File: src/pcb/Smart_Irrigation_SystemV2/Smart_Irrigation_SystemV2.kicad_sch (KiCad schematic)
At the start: 110 parts, among them J1 USB_C_Receptacle_USB2.0_16P, J2 FPC_Connector, J3 AudioJack3, J4 AudioJack3, J5 AudioJack3, J7 AudioJack3, J8 AudioJack3, J9 Battary Connection, Q1 MUN5211DW1, Q2 FDN340P, Q3 AO3400A, SW1 IO0 Switch, SW2 EN Switch, SW3 SW_Push, SW4 SW_Push, SW5 SW_Push, SW6 SW_Push, U1 CP2102N-Axx-xQFN28, U2 ESP32-WROOM-32, U3 ADS1115IDGS, U4 DS3231MZ, U5 TLV62568ADRL, U6 SN74LVC245APW, U7 TP4056-42-ESOP8, U8 TPS63001, U9 AT24CS32-SSHM

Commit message: set footprints, added TestPoints, searched JLCPCB Parts
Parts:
- added J10, J11, J6: I2C, Connector_PinSocket_2.54mm:PinSocket_1x04_P2.54mm_Vertical, symbol Connector:Conn_01x04_Socket
- added TP15: GND, TestPoint:TestPoint_Pad_2.5x2.5mm, symbol Connector:TestPoint
- added TP16: 3.3V, TestPoint:TestPoint_Pad_4.0x4.0mm, symbol Connector:TestPoint
- C1, C10, C11, C2, C4, C8, C9: footprint (none) -> Capacitor_SMD:C_0805_2012Metric; JLCPCB Part Number (none) -> C28233
- C12, C13, C14: footprint (none) -> Capacitor_SMD:C_0805_2012Metric; JLCPCB Part Number (none) -> C15850
- C3, C5, C6: footprint (none) -> Capacitor_SMD:C_0805_2012Metric; JLCPCB Part Number (none) -> C1779
- C7: footprint (none) -> Capacitor_SMD:C_0805_2012Metric; JLCPCB Part Number (none) -> C45783
- D1, D11, D12, D15, D16, D17, D2, D3: JLCPCB Part Number (none) -> C5274290
- D10: JLCPCB Part Number (none) -> C5355496
- D4: footprint Package_TO_SOT_SMD:SOT-23-5 -> Diode_SMD:D_SOD-323F; JLCPCB Part Number (none) -> C27636120
- D5, D6, D7: footprint LED_SMD:LED_Cree-XHP50_3V_HighDensity -> Diode_SMD:D_0603_1608Metric; JLCPCB Part Number (none) -> C2286
- D8: footprint LED_SMD:LED_Cree-XHP50_3V_HighDensity -> Diode_SMD:D_0603_1608Metric; JLCPCB Part Number (none) -> C2287
- D9: footprint LED_SMD:LED_Cree-XHP50_3V_HighDensity -> Diode_SMD:D_0603_1608Metric; JLCPCB Part Number (none) -> C12624
- H1, H2, H3, H4: footprint Module:Maple_Mini -> MountingHole:MountingHole_3.2mm_M3_DIN965_Pad
- J1: footprint Package_DFN_QFN:UQFN-16_1.8x2.6mm_P0.4mm -> Connector_USB:USB_C_Receptacle_HRO_TYPE-C-31-M-12; JLCPCB Part Number (none) -> C5337088
- J2: footprint Package_QFP:TQFP-144_20x20mm_P0.5mm -> 5051105091:CON_5051105091_MOL; JLCPCB Part Number (none) -> C779387
- J3, J4, J5, J7, J8: footprint Package_LCC:PLCC-84_29.3x29.3mm_P1.27mm -> (none); JLCPCB Part Number (none) -> C707248
- J9: footprint Package_QFP:TQFP-144_20x20mm_P0.5mm -> Connector_JST:JST_PH_B2B-PH-K_1x02_P2.00mm_Vertical
- L1: footprint Package_TO_SOT_SMD:SOT-563 -> Inductor_SMD:L_7.3x7.3_H3.5; JLCPCB Part Number (none) -> C726315
- L2: footprint Relay_THT:Relay_DPDT_Finder_30.22 -> Inductor_SMD:L_7.3x7.3_H3.5; JLCPCB Part Number (none) -> C128686
- MICRO_SD1: JLCPCB Part Number (none) -> C91145
- Q1: JLCPCB Part Number (none) -> C152507
- Q2: JLCPCB Part Number (none) -> C347510
- Q3: JLCPCB Part Number (none) -> C20917
- R1, R2: footprint Resistor_THT:R_Array_SIP4 -> Resistor_SMD:R_0805_2012Metric; JLCPCB Part Number (none) -> C26023
- R10, R11, R12, R13, R14, R15: footprint Resistor_THT:R_Array_SIP4 -> Resistor_SMD:R_0805_2012Metric; JLCPCB Part Number (none) -> C17415
- R16: footprint Resistor_THT:R_Array_SIP4 -> Resistor_SMD:R_0805_2012Metric; JLCPCB Part Number (none) -> C17477
- R17, R5: footprint Resistor_THT:R_Array_SIP4 -> Resistor_SMD:R_0805_2012Metric; JLCPCB Part Number (none) -> C17414
- R18, R19, R4: footprint (none) -> Resistor_SMD:R_0805_2012Metric; JLCPCB Part Number (none) -> C17673
- R20, R21, R22, R23: footprint Resistor_THT:R_Array_SIP4 -> Resistor_SMD:R_0805_2012Metric; JLCPCB Part Number (none) -> C17513
- R24: footprint (none) -> Resistor_SMD:R_0805_2012Metric; JLCPCB Part Number (none) -> C17414
- R25, R26, R27: footprint Package_SON:Texas_DRC0010J_ThermalVias -> Resistor_SMD:R_0805_2012Metric; JLCPCB Part Number (none) -> C17604
- R28: footprint Package_SON:Texas_DRC0010J_ThermalVias -> Resistor_SMD:R_0805_2012Metric; JLCPCB Part Number (none) -> C17408
- R29: footprint Package_SON:Texas_DRC0010J_ThermalVias -> Resistor_SMD:R_0805_2012Metric; JLCPCB Part Number (none) -> C25611
- R3: footprint Resistor_THT:R_Array_SIP4 -> Resistor_SMD:R_0805_2012Metric; JLCPCB Part Number (none) -> C17520
- R30, R31, R32: footprint Package_SON:Texas_DRC0010J_ThermalVias -> Resistor_SMD:R_0805_2012Metric; JLCPCB Part Number (none) -> C17414
- R33, R34: footprint (none) -> Resistor_SMD:R_0805_2012Metric; JLCPCB Part Number (none) -> C17477
- R6, R7: footprint (none) -> Resistor_SMD:R_0805_2012Metric; JLCPCB Part Number (none) -> C17513
- R8: footprint Resistor_THT:R_Array_SIP4 -> Resistor_SMD:R_0805_2012Metric; JLCPCB Part Number (none) -> C17702
- R9: footprint (none) -> Resistor_SMD:R_0805_2012Metric; JLCPCB Part Number (none) -> C25611
- SW1, SW2: footprint Button_Switch_THT:SW_NKK_GW12LJP -> (none); JLCPCB Part Number (none) -> C83206
- SW3, SW4, SW5, SW6: footprint Button_Switch_THT:SW_NKK_GW12LJP -> (none); JLCPCB Part Number (none) -> C49234238
- TP1: value TestPoint -> GPIO32; footprint Package_SO:TSSOP-16_4.4x5mm_P0.65mm -> TestPoint:TestPoint_Pad_D1.5mm
- TP10, TP11, TP12, TP13, TP14, TP4, TP5, TP6, TP7, TP8, TP9: footprint (none) -> TestPoint:TestPoint_Pad_D1.5mm
- TP2, TP3: footprint Package_SO:TSSOP-16_4.4x5mm_P0.65mm -> TestPoint:TestPoint_Pad_D1.5mm
- U1: JLCPCB Part Number (none) -> C964632
- U2: JLCPCB Part Number (none) -> C701343
- U3: JLCPCB Part Number (none) -> C37593
- U4: JLCPCB Part Number (none) -> C107410
- U5: JLCPCB Part Number (none) -> C87122
- U6: JLCPCB Part Number (none) -> C7848
- U7: JLCPCB Part Number (none) -> C16581
- U8: JLCPCB Part Number (none) -> C28060
- U9: JLCPCB Part Number (none) -> C615972
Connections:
- net +3.3V: now also J10.4 (Pin_4), J11.4 (Pin_4), J6.4 (Pin_4), TP16.1
- net GND: now also J10.3 (Pin_3), J11.3 (Pin_3), J6.3 (Pin_3), TP15.1
- net SCL: now also J10.1 (Pin_1), J11.1 (Pin_1), J6.1 (Pin_1)
- net SDA: now also J10.2 (Pin_2), J11.2 (Pin_2), J6.2 (Pin_2)

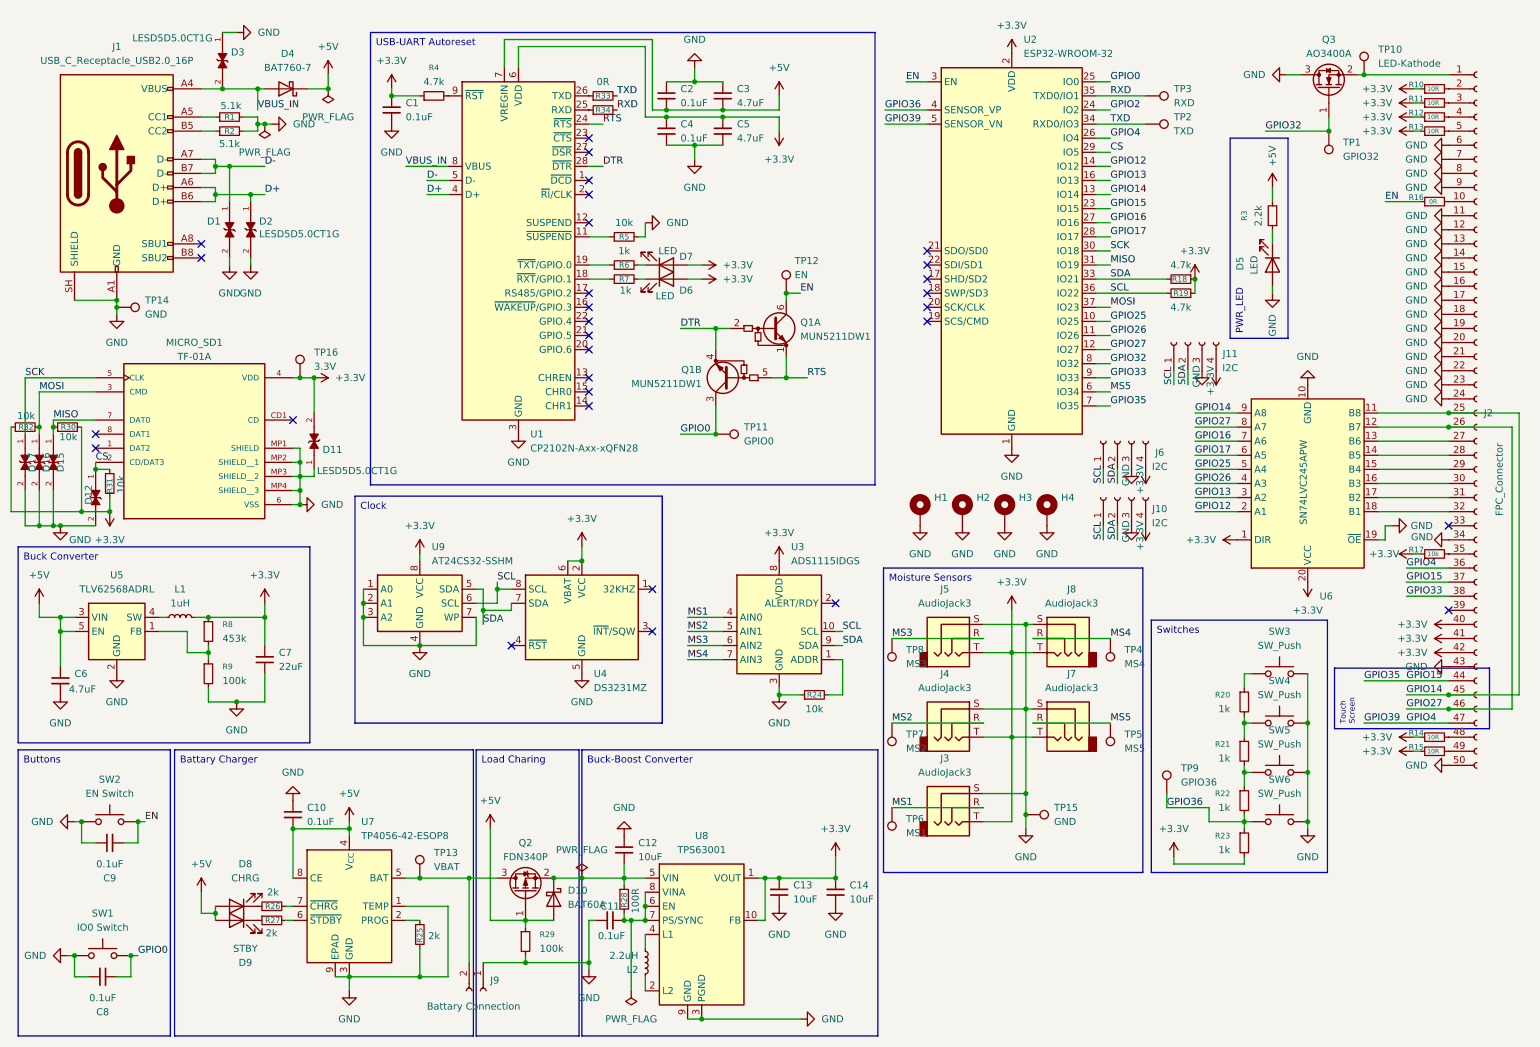
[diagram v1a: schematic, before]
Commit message: added battary voltage measurement and one more MS. selected footrints using easyeda2kicad and mapped the correct jlcpcb part number- need to find right connectors. worked about 2 hours
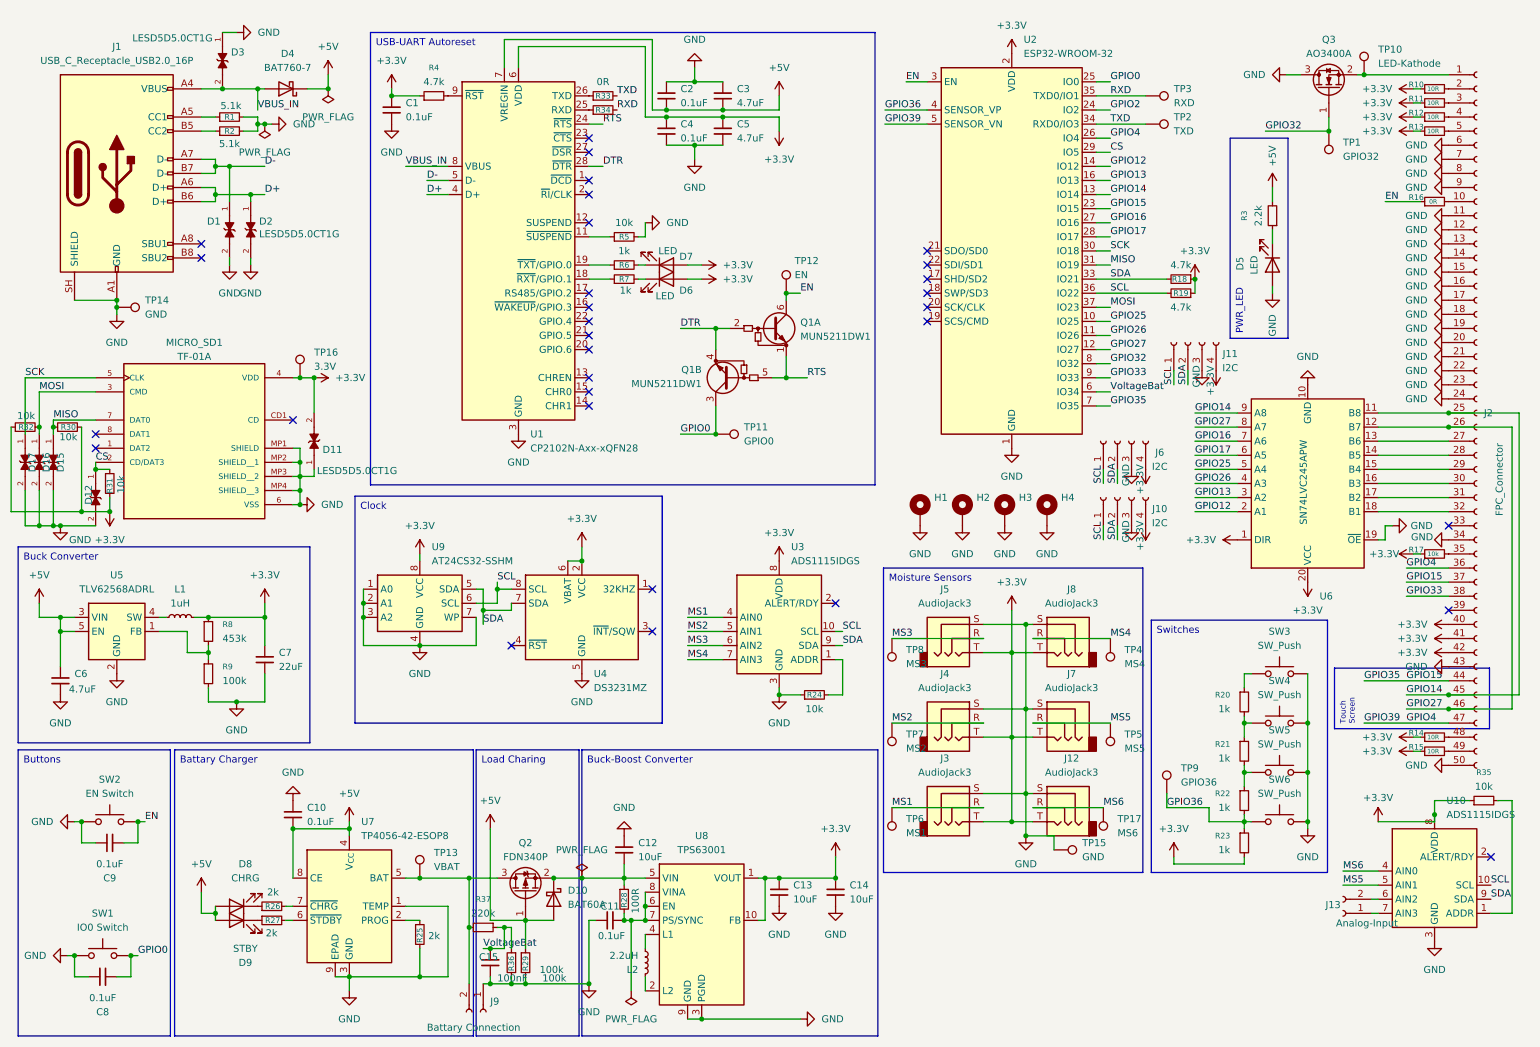
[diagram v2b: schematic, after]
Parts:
- added C15: 100nF, Capacitor_SMD:C_0805_2012Metric, symbol Device:C_Small
- added J12: AudioJack3, Test:AUDIO-TH_PJ-3136-3A, symbol Connector_Audio:AudioJack3
- added J13: Analog-Input, symbol Connector:Conn_01x02_Socket
- added R35: 10k, Resistor_SMD:R_0805_2012Metric, symbol Device:R_Small
- added R36: 100k, Resistor_SMD:R_0805_2012Metric, symbol Device:R_Small
- added R37: 220k, Resistor_SMD:R_0805_2012Metric, symbol Device:R_Small
- added TP17: MS6, Relay_THT:Relay_DPDT_Schrack-RT2-FormC_RM5mm, symbol Connector:TestPoint
- added U10: ADS1115IDGS, Package_SO:TSSOP-10_3x3mm_P0.5mm, symbol Analog_ADC:ADS1115IDGS
- J3, J4, J5, J7, J8: footprint (none) -> Test:AUDIO-TH_PJ-3136-3A
- SW1, SW2: footprint (none) -> Test:KEY-SMD_4P-L6.0-W6.0-P3.90-LS9.0
- SW3, SW4, SW5, SW6: footprint (none) -> Test:SW-TH_CPG151101D9X
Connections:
- net +3.3V: now also J12.T, R35.1, U10.8 (VDD)
- net GND: now also C15.2, J12.S, R36.2, U10.3 (GND)
- net MS5: now also U10.5 (AIN1); no longer U2.6 (IO34)
- net SCL: now also U10.10 (SCL)
- net SDA: now also U10.9 (SDA)
- net at J9.2 (Pin_2), Q2.3 (D), TP13.1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: now also R37.2
- new net: J13.1 (Pin_1), U10.7 (AIN3)
- new net: J13.2 (Pin_2), U10.6 (AIN2)
- new net: R35.2, U10.1 (ADDR)
- new net MS6: J12.R, TP17.1, U10.4 (AIN0)
- new net VoltageBat: C15.1, R36.1, R37.1, U2.6 (IO34)
- no-connect marks 30 -> 31
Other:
- moved on the sheet: J9, R29, TP15

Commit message: added Solar Panel
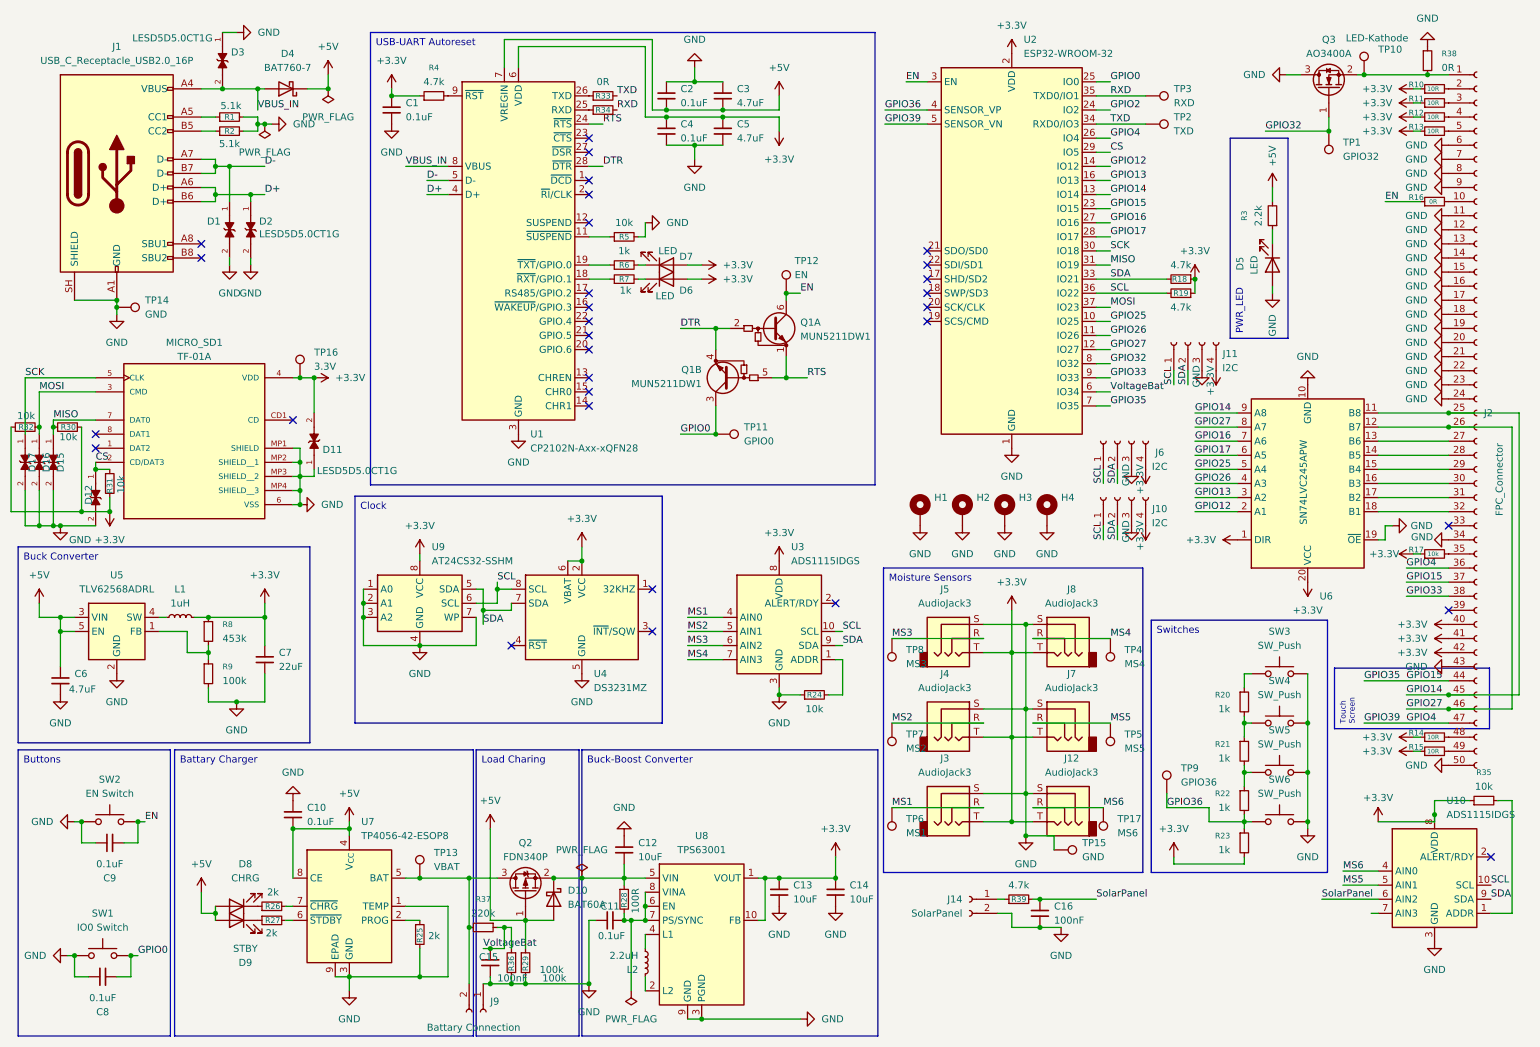
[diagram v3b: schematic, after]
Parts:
- removed J13: Analog-Input, symbol Connector:Conn_01x02_Socket
- added C16: 100nF, symbol Device:C_Small
- added J14: SolarPanel, symbol Connector:Conn_01x02_Socket
- added R38: 0R, Resistor_SMD:R_0805_2012Metric, symbol Device:R_Small
- added R39: 4.7k, Resistor_THT:R_Array_SIP4, symbol Device:R_Small
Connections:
- net GND: now also C16.2, J14.2 (Pin_2), R38.1
- net at J2.1 (Pin_1), Q3.2 (S), TP10.1: now also R38.2
- net SolarPanel: now reaches U10.6 (AIN2)
- net SolarPanel: now also C16.1, R39.2
- new net: J14.1 (Pin_1), R39.1
